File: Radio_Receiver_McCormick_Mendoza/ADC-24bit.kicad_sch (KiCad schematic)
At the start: 36 parts, among them J21 SDR Out, J30 Q_OUT, J31 Q_OUT, J32 Q_OUT, J41 V_DIV, J42 VDDA/2, U10 OPA1612AID, U12 PCM1808PWR

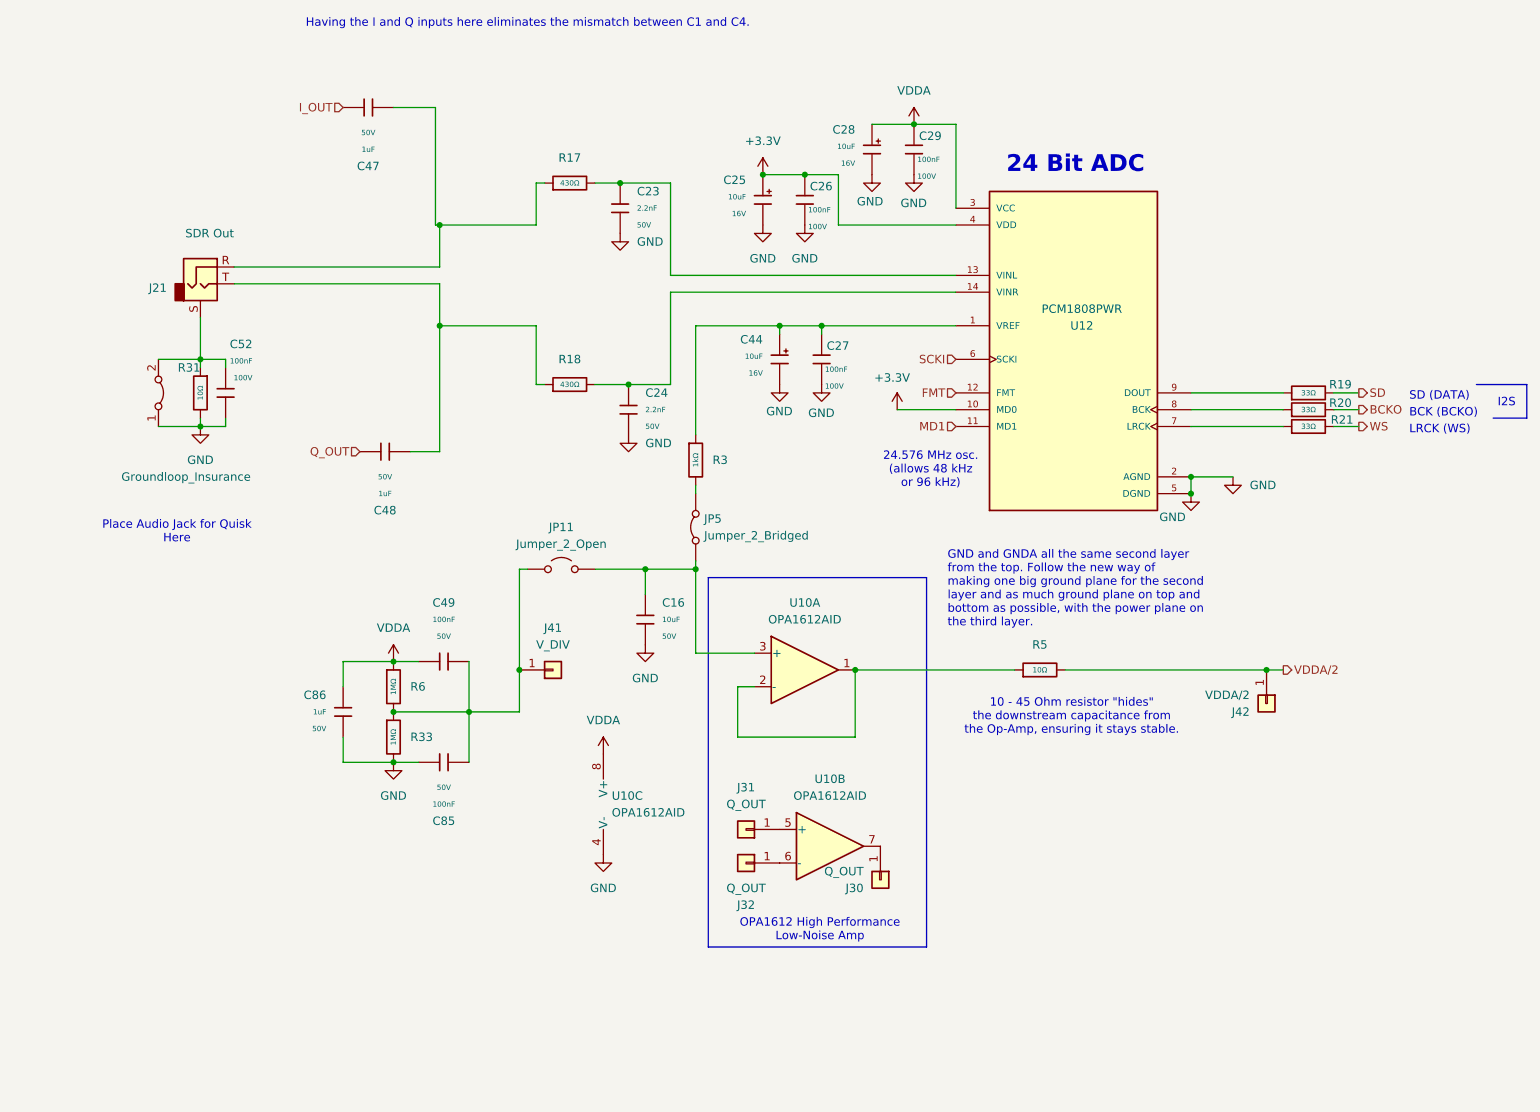
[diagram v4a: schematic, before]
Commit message: Created low mono, high stereo impedance DAC audio outlets
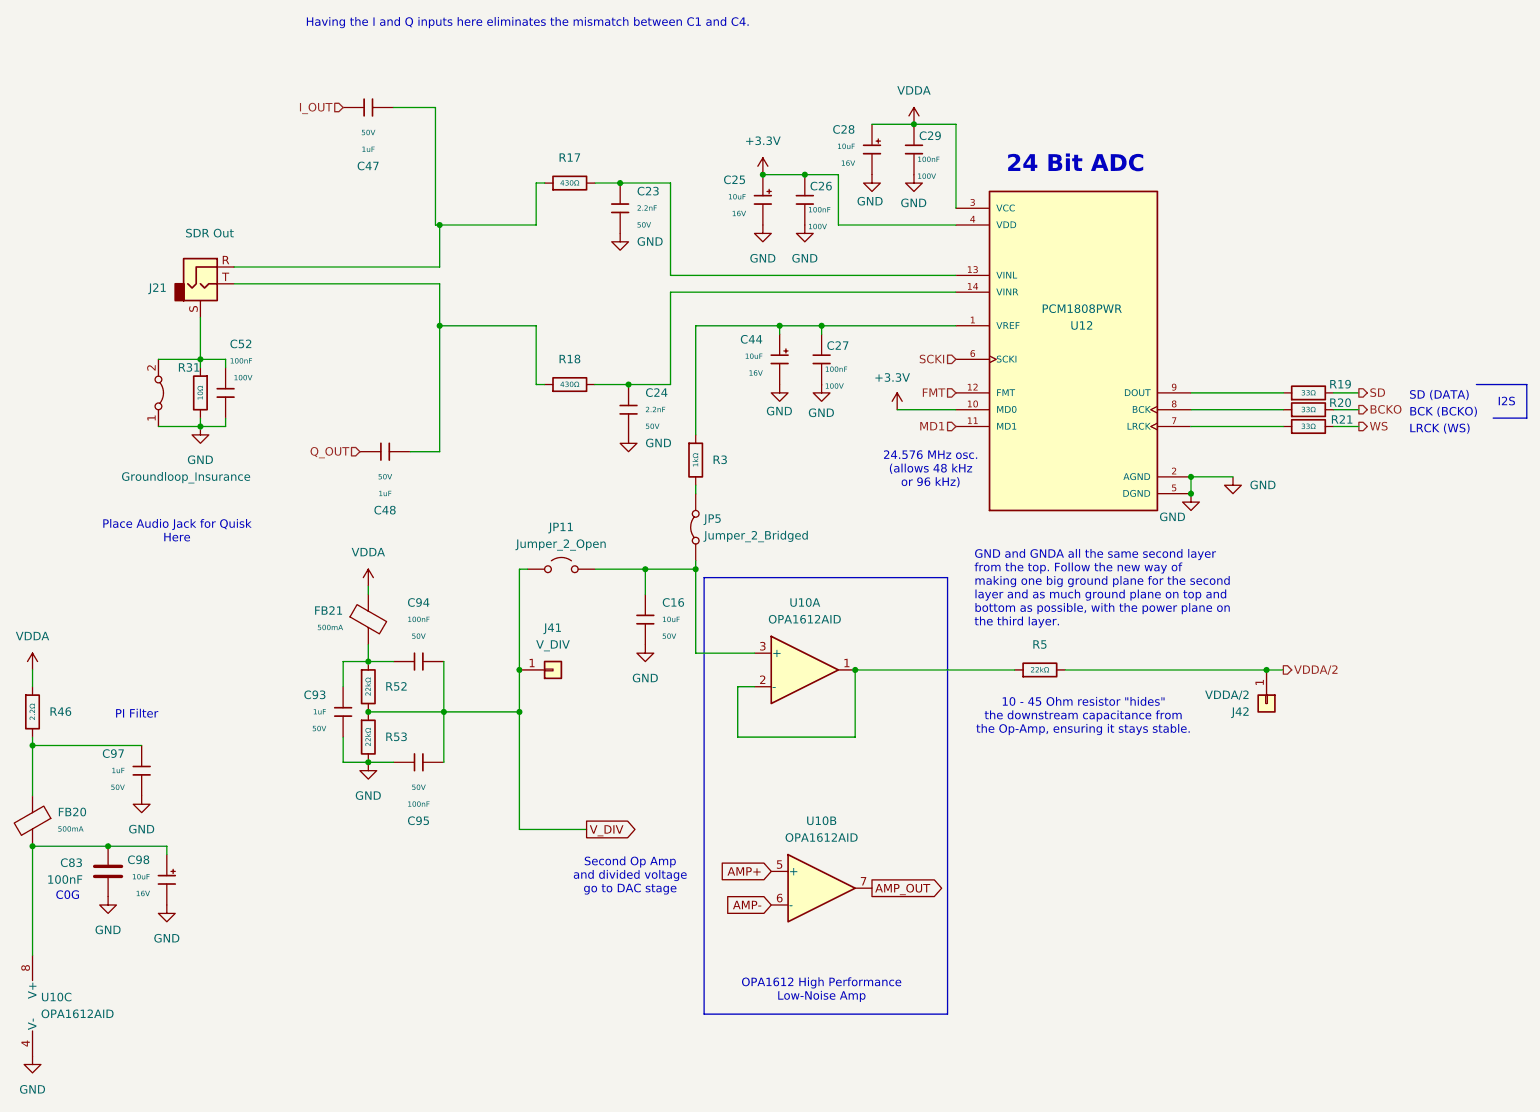
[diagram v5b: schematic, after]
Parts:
- removed C49, C85: 100nF, PCM_JLCPCB:C_0402, symbol PCM_JLCPCB-Capacitors:0402,100nF,(2)
- removed C86: 1uF, PCM_JLCPCB:C_0603, symbol PCM_JLCPCB-Capacitors:0603,1uF
- removed J30, J31, J32: Q_OUT, Connector_PinHeader_2.54mm:PinHeader_1x01_P2.54mm_Vertical, symbol Connector_Generic:Conn_01x01
- removed R33, R6: 1MΩ, PCM_JLCPCB:R_0603, symbol PCM_JLCPCB-Resistors:0603,1MΩ
- removed R5: 10Ω, PCM_JLCPCB:R_0805, symbol PCM_JLCPCB-Resistors:0805,10Ω
- added C83: 100nF, PCM_JLCPCB:C_1206, symbol Device:C
- added C93, C97: 1uF, PCM_JLCPCB:C_0603, symbol PCM_JLCPCB-Capacitors:0603,1uF
- added C94, C95: 100nF, PCM_JLCPCB:C_0402, symbol PCM_JLCPCB-Capacitors:0402,100nF,(2)
- added C98: 10uF, PCM_JLCPCB:C_CASE-A-3216-18(mm), symbol PCM_JLCPCB-Capacitors:CASE-A-3216-18(mm),10uF
- added FB20, FB21: (no value), PCM_JLCPCB:FB_0805, symbol PCM_JLCPCB-Inductors:Ferrite,0805,(2)
- added R46: 2.2Ω, PCM_JLCPCB:R_0805, symbol PCM_JLCPCB-Resistors:0805,2.2Ω
- added R5, R52, R53: 22kΩ, PCM_JLCPCB:R_0805, symbol PCM_JLCPCB-Resistors:0805,22kΩ
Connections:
- net GND: now also C83.2, C93.2, C95.1, C97.2, C98.2, R53.2
- net VDDA: now also FB21.1, R46.1; no longer U10.8 (V+)
- net VDDA/2: now also R5.2
- net V_DIV: now reaches J41.1 (Pin_1), JP11.1 (A)
- net V_DIV: now also C94.1, C95.2, R52.2, R53.1
- net AMP_OUT: now reaches U10.7
- net AMP+: now reaches U10.5 (+)
- net at U10.1, U10.2 (-): now also R5.1
- net AMP-: now reaches U10.6 (-)
- new net: C93.1, C94.2, FB21.2, R52.1
- new net: C83.1, C98.1, FB20.2, U10.8 (V+)
- new net: C97.1, FB20.1, R46.2
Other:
- note added: "C0G"
- note added: "PI Filter"
- note added: "Second Op Amp and divided voltage go to DAC stage"
- moved on the sheet: U10B, U10C

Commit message: Added MicroSD card and verified footprints
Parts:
- JP11: footprint (none) -> Jumper:SolderJumper-2_P1.3mm_Open_RoundedPad1.0x1.5mm
- JP5: footprint (none) -> Jumper:SolderJumper-2_P1.3mm_Bridged_RoundedPad1.0x1.5mm
- R46, R5, R52, R53: Manufacturer UNI-ROYAL(Uniroyal Elec) -> (none)
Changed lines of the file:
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@@
 			)
 		)
-		(property "Manufacturer" "UNI-ROYAL(Uniroyal Elec)"
-			(at 77.47 125.73 0)
-			(hide yes)
-			(show_name no)
-			(do_not_autoplace no)
-			(effects
-				(font
-					(size 1.27 1.27)
-				)
-			)
-		)
 		(property "Part" "0805W8F2202T5E"
 			(at 77.47 125.73 0)
@@
 			)
 		)
-		(property "Footprint" ""
+		(property "Footprint" "Jumper:SolderJumper-2_P1.3mm_Open_RoundedPad1.0x1.5mm"
 			(at 106.68 107.95 0)
 			(hide yes)
@@
 			)
 		)
-		(property "Manufacturer" "UNI-ROYAL(Uniroyal Elec)"
-			(at 179.07 123.19 0)
-			(hide yes)
-			(show_name no)
-			(do_not_autoplace no)
-			(effects
-				(font
-					(size 1.27 1.27)
-				)
-			)
-		)
 		(property "Part" "0805W8F2202T5E"
 			(at 179.07 123.19 0)
@@
 			)
 		)
-		(property "Manufacturer" "UNI-ROYAL(Uniroyal Elec)"
-			(at 77.47 133.35 0)
-			(hide yes)
-			(show_name no)
-			(do_not_autoplace no)
-			(effects
-				(font
-					(size 1.27 1.27)
-				)
-			)
-		)
 		(property "Part" "0805W8F2202T5E"
 			(at 77.47 133.35 0)
@@
 			)
 		)
-		(property "Footprint" ""
+		(property "Footprint" "Jumper:SolderJumper-2_P1.3mm_Bridged_RoundedPad1.0x1.5mm"
 			(at 127 101.6 0)
 			(hide yes)
@@
 			(at 26.67 129.54 0)
 			(hide yes)
-			(show_name no)
-			(do_not_autoplace no)
-			(effects
-				(font
-					(size 1.27 1.27)
-				)
-			)
-		)
-		(property "Manufacturer" "UNI-ROYAL(Uniroyal Elec)"
-			(at 26.67 129.54 0)
-			(hide yes)

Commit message: Updated footprints
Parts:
- J21: footprint Intro_to_CAD:Jack_3.5mm_CUI_SJ-3523-SMT_Horizontal -> Reciever_Parts:Jack_3.5mm_CUI_SJ-3523-SMT_Horizontal
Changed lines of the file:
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@@
 			)
 		)
-		(property "Footprint" "Intro_to_CAD:Jack_3.5mm_CUI_SJ-3523-SMT_Horizontal"
+		(property "Footprint" "Reciever_Parts:Jack_3.5mm_CUI_SJ-3523-SMT_Horizontal"
 			(at 52.07 64.77 0)
 			(hide yes)

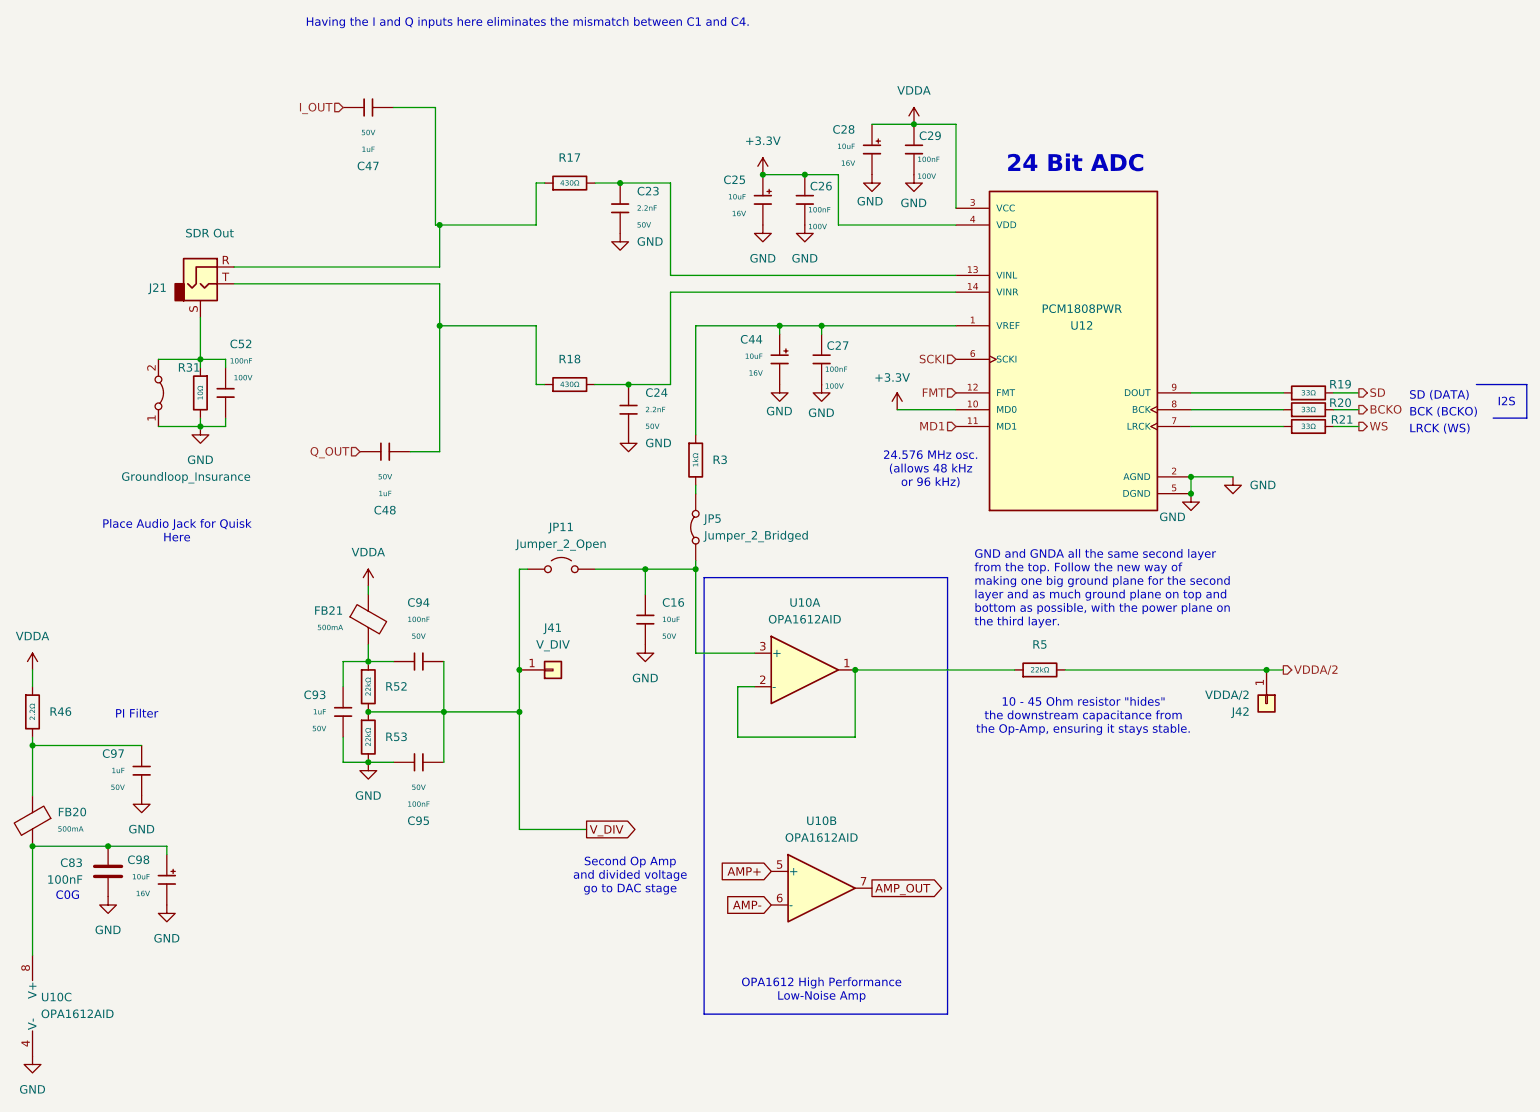
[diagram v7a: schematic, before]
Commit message: Routed antenna and isolated GNDA
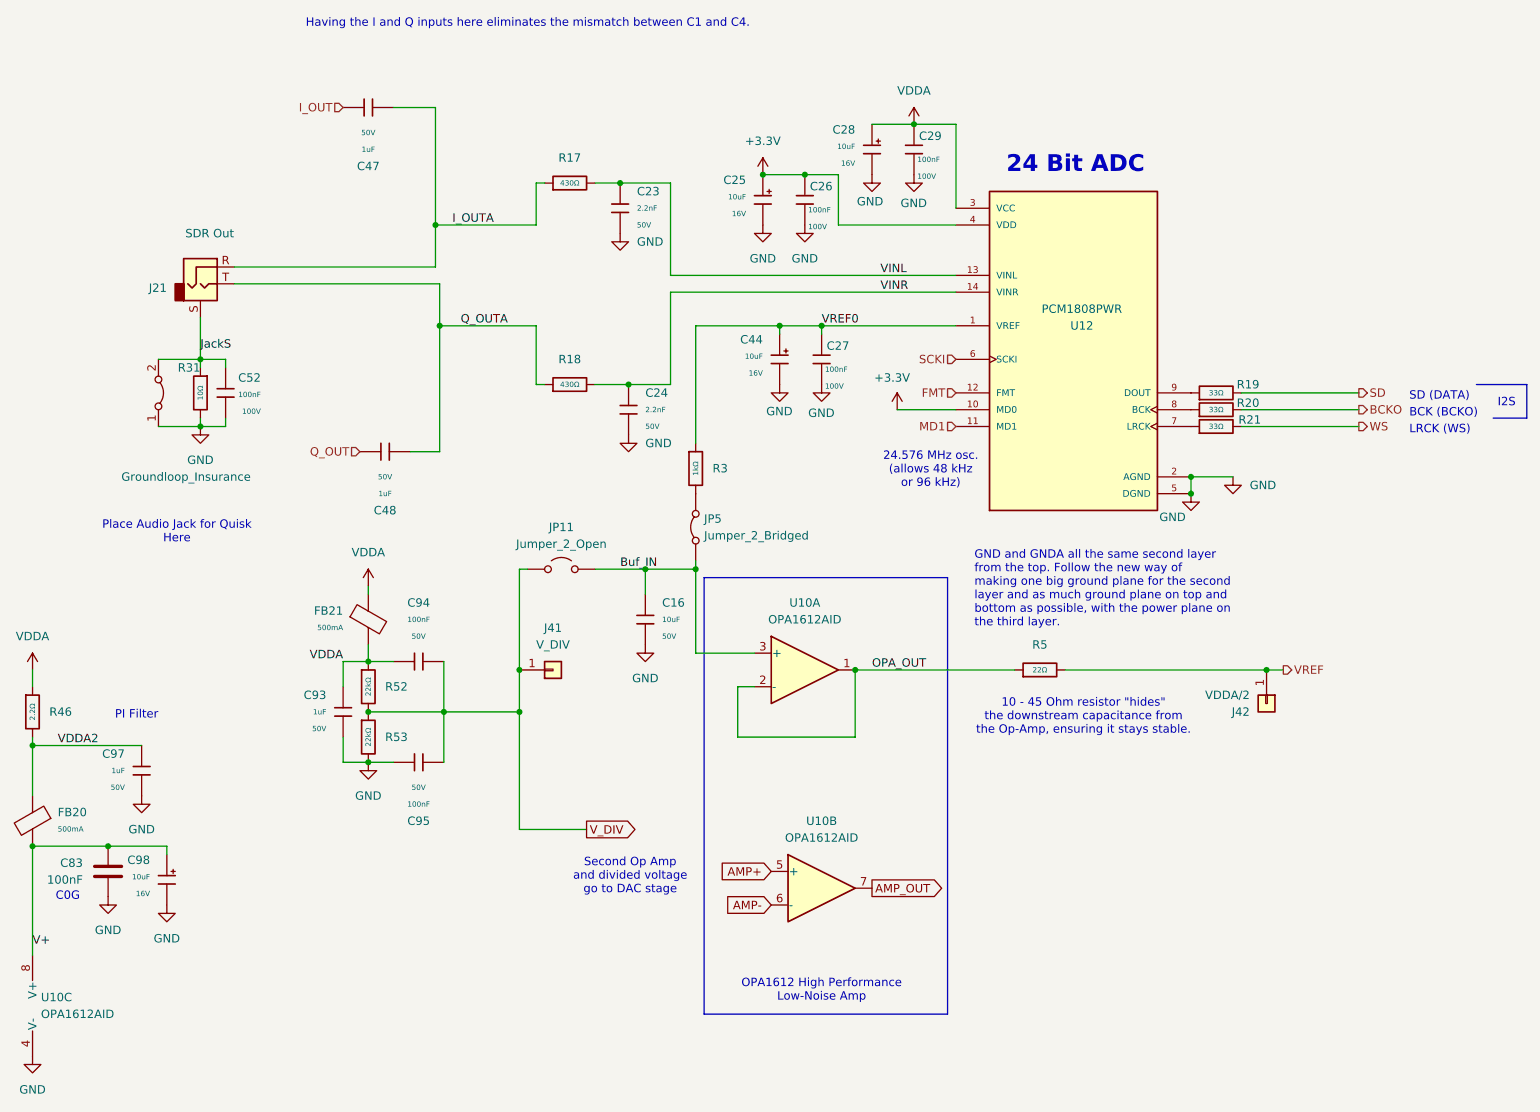
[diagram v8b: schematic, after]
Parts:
- removed R5: 22kΩ, PCM_JLCPCB:R_0805, symbol PCM_JLCPCB-Resistors:0805,22kΩ
- added R5: 22Ω, PCM_JLCPCB:R_0603, symbol PCM_JLCPCB-Resistors:0603,22Ω
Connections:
- net VDDA: now also C93.1, C94.2, FB21.2, R52.1
- net JackS: now reaches C52.2, J21.S, R31.1, e5.2 (B)
- net V+: now reaches C83.1, C98.1, FB20.2, U10.8 (V+)
- net VINL: now reaches C23.1, R17.2, U12.13 (VINL)
- net Q_OUTA: now reaches C48.1, J21.T, R18.1
- net VINR: now reaches C24.1, R18.2, U12.14 (VINR)
- net Buf_IN: now reaches C16.1, JP11.2 (B), JP5.1 (A), U10.3 (+)
- net VDDA2: now reaches C97.1, FB20.1, R46.2
- net I_OUTA: now reaches C47.1, J21.R, R17.1
- net VREF0: now reaches C27.2, C44.1, R3.1, U12.1 (VREF)
- net OPA_OUT: now reaches U10.1, U10.2 (-)
- net OPA_OUT: now also R5.1
- net VDDA/2 renamed VREF
- net VREF: now also R5.2
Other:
- moved on the sheet: R19, R20, R21, R3
